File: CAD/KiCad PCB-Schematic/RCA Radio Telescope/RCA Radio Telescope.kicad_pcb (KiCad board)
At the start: 2 copper layers, 2 parts, among them U3 SKY13588-460LF, U4 SKY13588-460LF

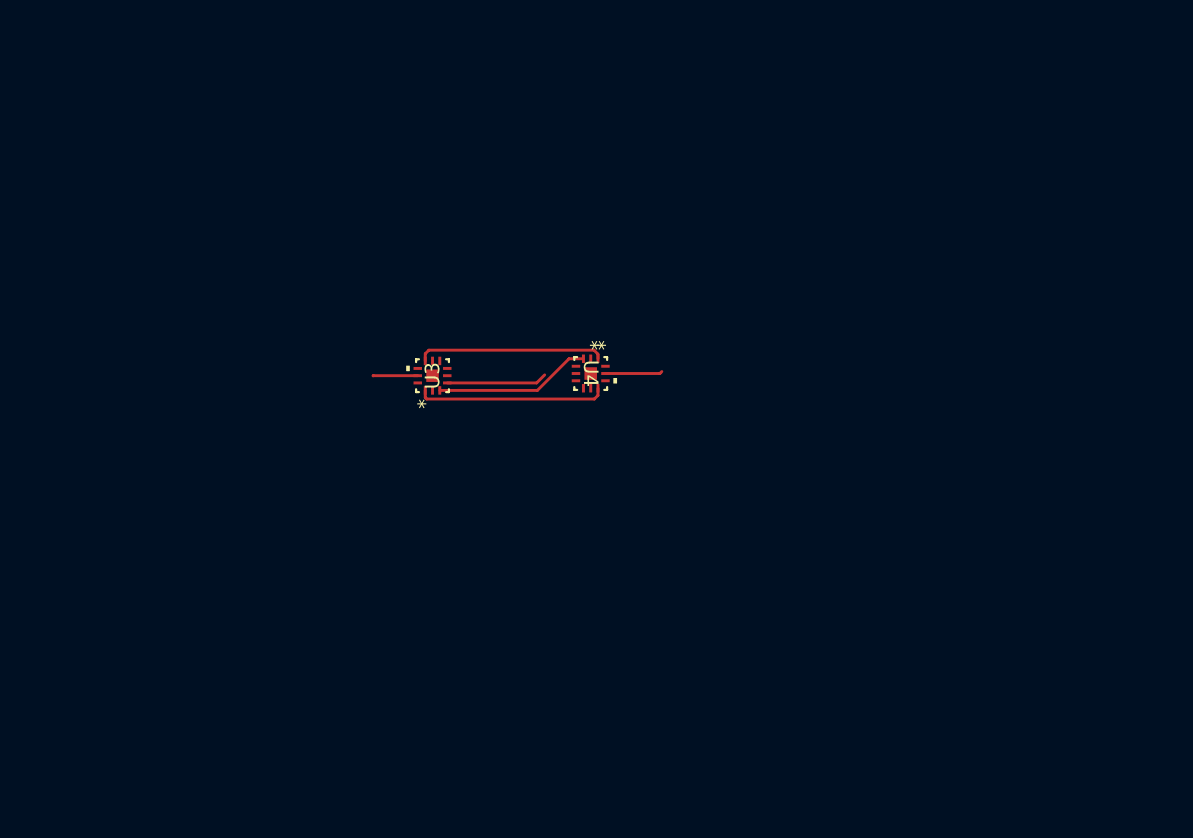
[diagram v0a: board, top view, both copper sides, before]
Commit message: Updated PowerDataDistribute schematicto v1.4
- Added components for fuses and PMOS
- Created PCB v1.0
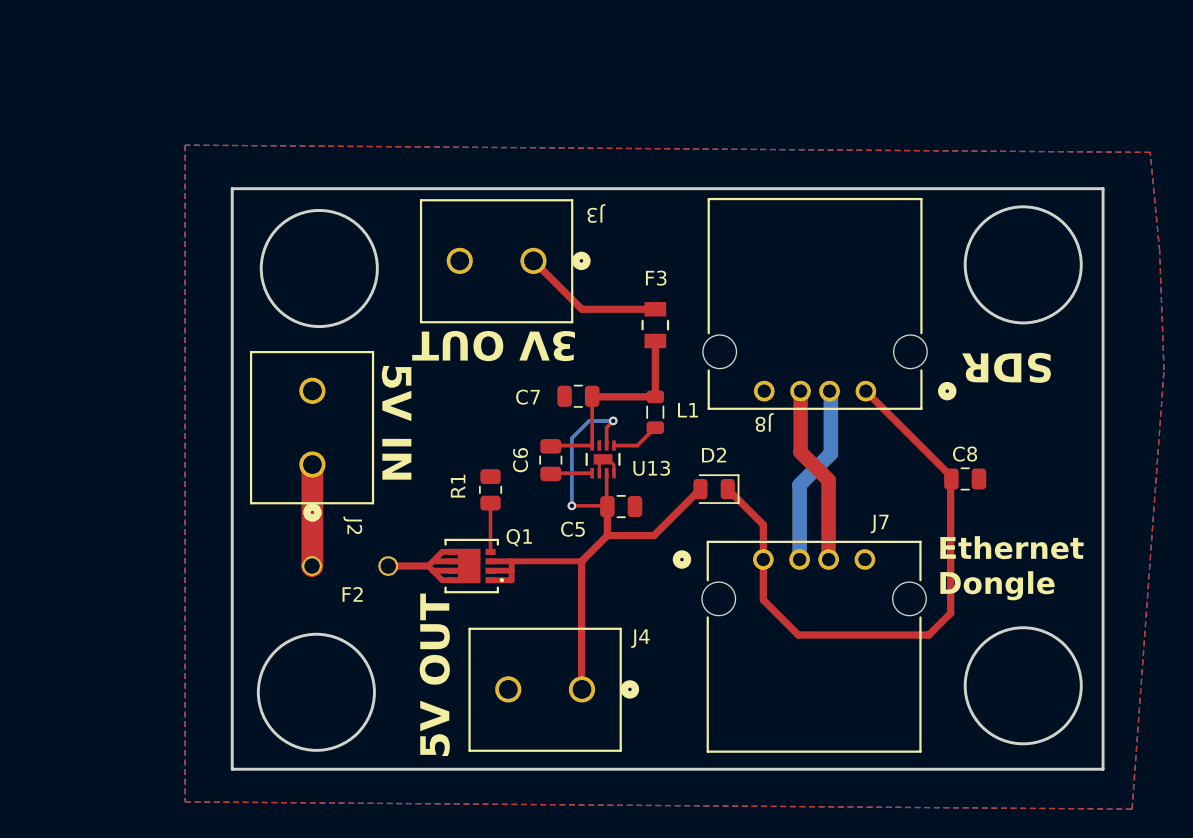
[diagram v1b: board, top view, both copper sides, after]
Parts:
- removed U3, U4: SKY13588-460LF, Library:QFN12_SKY
- added C5: 4.7 uF, Capacitor_SMD:C_0805_2012Metric, F.Cu at (52.3, 43.9)
- added C6: 560 pF, Capacitor_SMD:C_0805_2012Metric, F.Cu at (47.5, 40.7)
- added C7: 4.7 uF, Capacitor_SMD:C_0805_2012Metric, F.Cu at (49.4, 36.3)
- added C8: 10 uF, Capacitor_SMD:C_0805_2012Metric, F.Cu at (76.0, 42.0)
- added D2: D, Diode_SMD:D_0805_2012Metric, F.Cu at (58.7, 42.7)
- added F2: RGEF300K-2, Library:RGEF300K-2, F.Cu at (34.0, 52.0)
- added F3: 0ZCK0020FF2G, Library:0ZCK_BEL, F.Cu at (54.6, 31.4)
- added G***: LOGO, Library:dish, B.Cu at (46.4, 42.8)
- added J2: 5V From PoE Splitter, Library:CONN_1729128_PXC, F.Cu at (31.0, 41.0)
- added J3: 3V Out For LNA, Library:CONN_1729128_PXC, F.Cu at (46.3, 27.0)
- added J4: 5V Out For Filter Board, Library:CONN_1729128_PXC, F.Cu at (49.6, 56.5)
- added J7: USB_A, Library:CONN_AU-Y1005-2_ASM, F.Cu at (62.1, 47.6)
- added J8: USB_A, Library:CONN_AU-Y1005-2_ASM, F.Cu at (69.2, 35.9)
- added L1: 1 uH, Inductor_SMD:L_0805_2012Metric, F.Cu at (54.6, 37.4)
- added Q1: DMP2008UFG-7, Library:DMP2008UFG-7_DIO, F.Cu at (42.0, 48.0)
- added R1: 100k, Resistor_SMD:R_0805_2012Metric, F.Cu at (43.3, 42.8)
- added U13: MIC23050-SYML-TR, Library:MLF-8_ML_MCH, F.Cu at (51.0, 40.7)
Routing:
- net +5V: track 0.00 -> 45.8 mm, vias 0 -> 2
- net /PowerDataDistribute/USB_5V_IN: track 0.00 -> 40.9 mm
- net Net-(U13-SNS): track 0.00 -> 14.7 mm
- net /Filters/FILTERA_IN: track 13.0 -> 0.00 mm
- net /Filters/FILTERB_IN: track 12.9 -> 0.00 mm
- net /PowerDataDistribute/USB_D-_IN: track 0.00 -> 12.5 mm
- net /PowerDataDistribute/USB_D+_IN: track 0.00 -> 12.4 mm
- net /Filters/FILTERC_IN: track 10.8 -> 0.00 mm
- net Net-(Q1-D): track 0.00 -> 10.6 mm
- net +3V0: track 0.00 -> 9.77 mm
- net /PowerDataDistribute/VDD: track 0.00 -> 7.04 mm
- net /Filters/INT_CTRL_V1: track 6.94 -> 0.00 mm
- net /Filters/FILTER_OUT: track 3.94 -> 0.00 mm
- net Net-(Q1-G): track 0.00 -> 3.36 mm
- net Net-(U13-SW): track 0.00 -> 3.36 mm
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- added copper zone on B.Cu, net GND
- added copper zone on F.Cu, net GND
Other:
- board outline added: 60 x 40 mm
- board text added: "3V OUT"
- board text added: "5V IN"
- board text added: "5V OUT"
- board text added: "Ethernet Dongle"
- board text added: "PSU ECE Capstone Team 11 - RCA Telescope v1.0"
- board text added: "SDR"
- board text added: "Truong Le Brad Glaubitz Daniyil Kashkan Davyd Gamza Paul Nguyen"

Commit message: Updated Power/Data Distribute Board to v1.1
- Adjusted screw hole positions
- Adjusted screw terminal positions
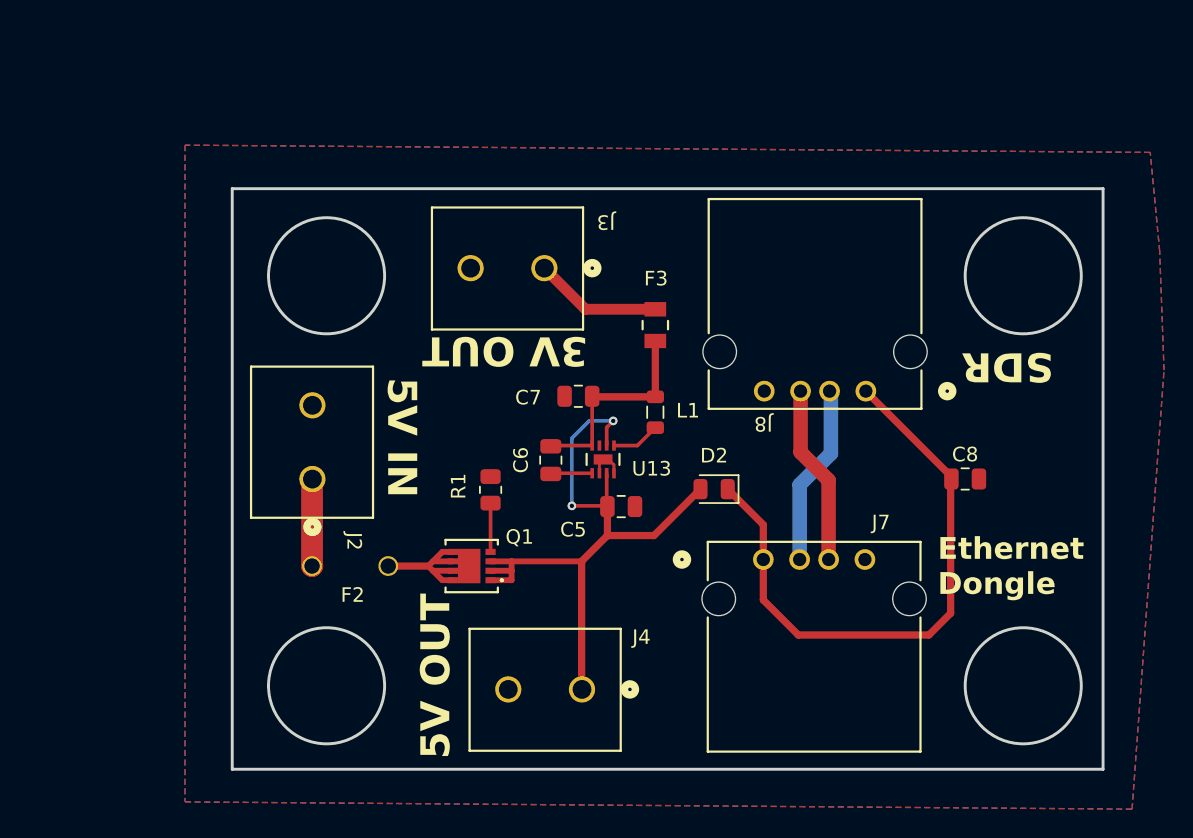
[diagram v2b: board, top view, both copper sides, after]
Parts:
- moved J2 1.00 mm to (31.0, 42.0)
- moved J3 0.90 mm to (47.0, 27.5)
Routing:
- net /PowerDataDistribute/VDD: track 7.04 -> 6.07 mm
- net +3V0: track 9.77 -> 8.82 mm
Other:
- outline, holes or cut-outs redrawn
- board text added: "PSU ECE Capstone Team 11 - RCA Telescope v1.1"
- board text removed: "PSU ECE Capstone Team 11 - RCA Telescope v1.0"
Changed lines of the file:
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@@
 		(title "Power Data Distribute PCB")
 		(date "2025-03-15")
-		(rev "1.0")
+		(rev "1.1")
 	)
 	(layers
@@
 		)
 		(property "Footprint" "Library:CONN_AU-Y1005-2_ASM"
-			(at 0 0 360)
+			(at 0 0 0)
 			(layer "F.Fab")
 			(hide yes)
@@
 		)
 		(property "Datasheet" ""
-			(at 0 0 360)
+			(at 0 0 0)
 			(layer "F.Fab")
 			(hide yes)
@@
 		)
 		(property "Description" ""
-			(at 0 0 360)
+			(at 0 0 0)
 			(layer "F.Fab")
 			(hide yes)
@@
 		(tags "capacitor")
 		(property "Reference" "C7"
-			(at 3.45 -0.0975 360)
+			(at 3.45 -0.0975 0)
 			(layer "F.SilkS")
 			(effects
@@
 		)
 		(property "Value" "4.7 uF"
-			(at 0 1.68 360)
+			(at 0 1.68 0)
 			(layer "F.Fab")
 			(effects
@@
 		)
 		(fp_text user "${REFERENCE}"
-			(at 0 0 360)
+			(at 0 0 0)
 			(layer "F.Fab")
 			(effects
@@
 		(tags "diode")
 		(property "Reference" "D2"
-			(at 0 2.3 360)
+			(at 0 2.3 0)
 			(layer "F.SilkS")
 			(effects
@@
 		)
 		(property "Value" "D"
-			(at 0 1.65 360)
+			(at 0 1.65 0)
 			(layer "F.Fab")
 			(effects
@@
 		)
 		(fp_text user "${REFERENCE}"
-			(at 0 0 360)
+			(at 0 0 0)
 			(layer "F.Fab")
 			(effects
@@
 		)
 		(property "Footprint" "Library:DMP2008UFG-7_DIO"
-			(at 0 0 360)
+			(at 0 0 0)
 			(layer "F.Fab")
 			(hide yes)
@@
 		)
 		(property "Datasheet" "https://ngspice.sourceforge.io/docs/ngspice-html-manual/manual.xhtml#cha_MOSFETs"
-			(at 0 0 360)
+			(at 0 0 0)
 			(layer "F.Fab")
 			(hide yes)
@@
 		)
 		(property "Description" "P-MOSFET transistor, drain/source/gate"
-			(at 0 0 360)
+			(at 0 0 0)
 			(layer "F.Fab")
 			(hide yes)
@@
 	(footprint "Library:CONN_1729128_PXC"
 		(layer "F.Cu")
-		(at 31.025 41.0066 90)
+		(at 31.025 42.0066 90)
 		(tags "1729128 ")
 		(property "Reference" "J2"
@@
 		)
 		(property "Footprint" "Library:CONN_1729128_PXC"
-			(at 0 0 360)
+			(at 0 0 0)
 			(layer "F.Fab")
 			(hide yes)
@@
 		)
 		(property "Datasheet" ""
-			(at 0 0 360)
+			(at 0 0 0)
 			(layer "F.Fab")
 			(hide yes)
@@
 		)
 		(property "Description" "Generic screw terminal, single row, 01x02, script generated (kicad-library-utils/schlib/autogen/connector/)"
-			(at 0 0 360)
+			(at 0 0 0)
 			(layer "F.Fab")
 			(hide yes)
@@
 	(footprint "Library:CONN_1729128_PXC"
 		(layer "F.Cu")
-		(at 46.2566 26.975001 180)
+		(at 47.0066 27.475001 180)
 		(tags "1729128 ")
 		(property "Reference" "J3"
@@
 		)
 		(property "Footprint" "Library:CONN_1729128_PXC"
-			(at 0 0 360)
+			(at 0 0 0)
 			(layer "F.Fab")
 			(hide yes)
@@
 		)
 		(property "Datasheet" ""
-			(at 0 0 360)
+			(at 0 0 0)
 			(layer "F.Fab")
 			(hide yes)
@@
 		)
 		(property "Description" "Generic screw terminal, single row, 01x02, script generated (kicad-library-utils/schlib/autogen/connector/)"
-			(at 0 0 360)
+			(at 0 0 0)
 			(layer "F.Fab")
 			(hide yes)
@@
 		(tags "capacitor")
 		(property "Reference" "C5"
-			(at -3.3 1.5975 360)
+			(at -3.3 1.5975 0)
 			(layer "F.SilkS")
 			(effects
@@
 		)
 		(property "Value" "4.7 uF"
-			(at 0.95 2.68 360)
+			(at 0.95 2.68 0)
 			(layer "F.Fab")
 			(effects
@@
 		)
 		(fp_text user "${REFERENCE}"
-			(at -3.55 2.18 360)
+			(at -3.55 2.18 0)
 			(layer "F.Fab")
 			(effects
@@
 		(tags "capacitor")
 		(property "Reference" "C8"
-			(at 0 -1.68 360)
+			(at 0 -1.68 0)
 			(layer "F.SilkS")
 			(effects
@@
 		)
 		(property "Value" "10 uF"
-			(at 0 1.68 360)
+			(at 0 1.68 0)
 			(layer "F.Fab")
 			(effects
@@
 		)
 		(fp_text user "${REFERENCE}"
-			(at 0 0 360)
+			(at 0 0 0)
 			(layer "F.Fab")
 			(effects
@@
 	)
 	(gr_circle
-		(center 31.5 27.5)
-		(end 35.5 27.5)
+		(center 32 28)
+		(end 36 28)
 		(stroke
 			(width 0.2)
@@
 	)
 	(gr_circle
-		(center 80 27.25)
-		(end 84 27.25)
+		(center 80 28)
+		(end 84 28)
 		(stroke
 			(width 0.2)
@@
 	)
 	(gr_circle
-		(center 31.3 56.7)
-		(end 27.3 56.7)
+		(center 32 56.25)
+		(end 28 56.25)
 		(stroke
 			(width 0.2)
@@
 		(layer "Edge.Cuts")
 	)
-	(gr_text "PSU ECE Capstone\nTeam 11 - RCA Telescope\nv1.0"
+	(gr_text "PSU ECE Capstone\nTeam 11 - RCA Telescope\nv1.1"
 		(at 70.3 32.8 0)
 		(layer "B.SilkS")
@@
 	)
 	(gr_text "5V IN"
-		(at 35.6 34 -90)
+		(at 36 35 -90)
 		(layer "F.SilkS")
 		(effects
@@
 	)
 	(gr_text "3V OUT"
-		(at 49.3 31.6 180)
+		(at 50 32 180)
 		(layer "F.SilkS")
 		(effects
@@
 		)
 	)
+	(dimension
+		(type aligned)
+		(layer "F.SilkS")
+		(pts
+			(xy 32 28) (xy 80 28)
+		)
+		(height 28.25)
+		(gr_text "48.0000 mm"
+			(at 56 55.15 0)
+			(layer "F.SilkS")
+			(effects
+				(font
+					(size 1 1)
+					(thickness 0.1)
+				)
+			)
+		)
+		(format
+			(prefix "")
+			(suffix "")
+			(units 3)
+			(units_format 1)
+			(precision 4)
+		)
+		(style
+			(thickness 0.1)
+			(arrow_length 1.27)
+			(text_position_mode 0)
+			(extension_height 0.58642)
+			(extension_offset 0.5) keep_text_aligned)
+	)
 	(segment
 		(start 51.800001 41.022401)
@@
 	)
 	(segment
-		(start 46.2566 26.975001)
-		(end 49.589399 30.3078)
-		(width 0.5)
+		(start 49.839399 30.3078)
+		(end 47.0066 27.475001)
+		(width 0.75)
 		(layer "F.Cu")
 		(net 3)
 	)
 	(segment
-		(start 49.589399 30.3078)
-		(end 54.65 30.3078)
-		(width 0.5)
+		(start 54.65 30.3078)
+		(end 49.839399 30.3078)
+		(width 0.75)
 		(layer "F.Cu")
 		(net 3)
@@
 	)
 	(segment
-		(start 31.025 41.0066)
-		(end 31.025 47.975)
+		(start 31 42.0316)
+		(end 31.025 42.0066)
+		(width 1.5)
+		(layer "F.Cu")
+		(net 10)
+	)
+	(segment
+		(start 31 48)
+		(end 31 42.0316)
 		(width 1.5)
 		(layer "F.Cu")

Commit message: Updated PowerData Board to v1.2
- Added zone fills for certain pins
- Added ground vias for mounting holes
- Minor readjustments to components
- Added silkscreen for voltage polarity
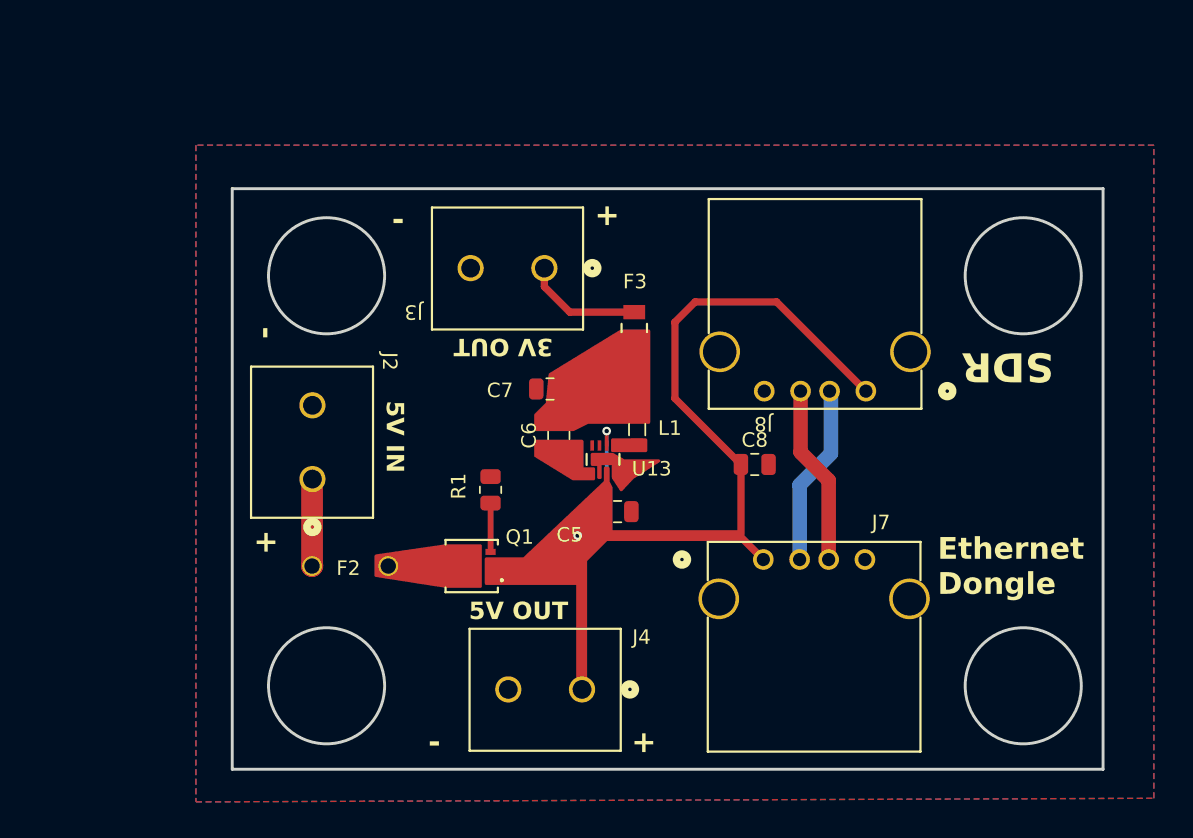
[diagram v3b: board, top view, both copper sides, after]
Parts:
- removed D2: D, Diode_SMD:D_0805_2012Metric
- moved C8 14.5 mm to (61.5, 41.0)
- moved C7 2.01 mm to (47.4, 35.8)
- moved C6 1.79 mm to (48.0, 39.0)
- moved L1 1.73 mm to (53.4, 38.6)
- moved F3 1.46 mm to (53.2, 31.6)
- moved C5 0.43 mm to (52.0, 44.2)
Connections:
- C8 pad 1: /PowerDataDistribute/USB_5V_IN -> +5V
- J7 pad 1: /PowerDataDistribute/USB_5V_IN -> +5V
- J8 pad 1: /PowerDataDistribute/USB_5V_IN -> +5V
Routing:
- net /PowerDataDistribute/USB_5V_IN: track 40.9 -> 0.00 mm
- net +5V: track 45.8 -> 66.5 mm
- net Net-(U13-SNS): track 14.7 -> 0.00 mm
- net Net-(Q1-D): track 10.6 -> 0.00 mm
- net Net-(U13-SW): track 3.36 -> 0.00 mm
- net Net-(U13-CFF): track 2.94 -> 0.00 mm
- net GND: track 2.54 -> 0.38 mm
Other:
- board text added: "+"
- board text added: "-"

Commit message: Updated Power Data Distribute PCB to v1.3
- Rearranged 5 to 3V PCB layout to fit new circuit
- Added via stitching to PCB
- Added some constraints supplied by JLCPCB
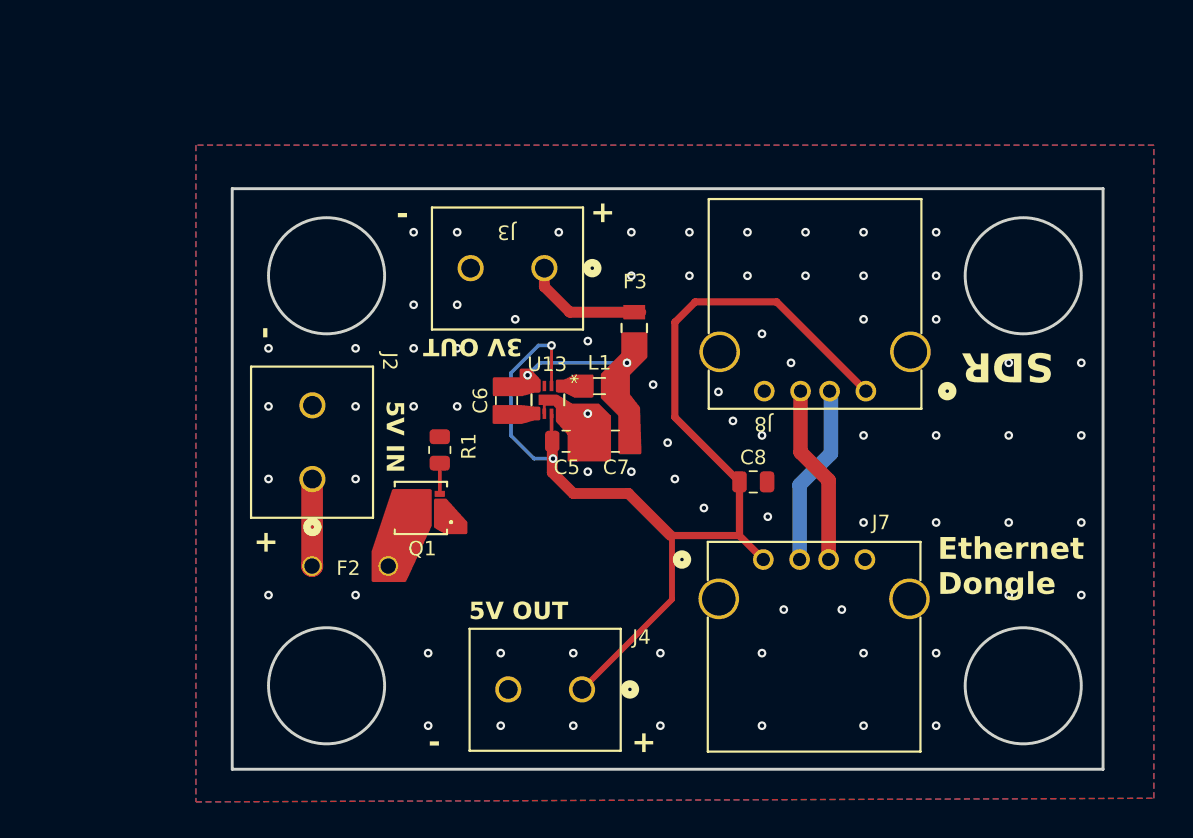
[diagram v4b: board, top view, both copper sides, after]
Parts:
- moved C5 6.01 mm to (48.5, 39.4)
- moved C7 5.76 mm to (51.9, 39.4)
- moved U13 5.59 mm to (47.2, 36.5)
- moved Q1 5.32 mm to (38.5, 44.0)
- moved R1 4.45 mm to (39.8, 40.0)
- moved C6 4.33 mm to (44.4, 36.6)
- moved L1 3.97 mm to (50.8, 35.6), turned to 0 degrees
- moved C8 1.20 mm to (61.4, 42.2)
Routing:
- net +5V: track 66.5 -> 81.2 mm
- net Net-(U13-SNS): track 0.00 -> 7.20 mm, vias 0 -> 2
- net Net-(Q1-G): track 3.36 -> 2.11 mm
- net GND: track 0.38 -> 1.44 mm, vias 0 -> 74

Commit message: V1.5 Schematic and 1.4 PCB Layout
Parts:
- added C10: 0.1uF, Capacitor_SMD:C_0805_2012Metric, F.Cu at (44.5, 48.0)
- added C11: 3.3nF, Capacitor_SMD:C_0805_2012Metric, F.Cu at (44.5, 44.2)
- added C12: 22uF, Capacitor_SMD:C_0805_2012Metric, F.Cu at (47.6, 49.4)
- added C9: 10uF, Capacitor_SMD:C_0805_2012Metric, F.Cu at (41.1, 48.0)
- added L2: 2.2uH, Inductor_SMD:L_0805_2012Metric, F.Cu at (50.5, 48.6)
- added R2: 100k, Resistor_SMD:R_0805_2012Metric, F.Cu at (51.4, 45.7)
- added U14: TPS62133RGTR, TPS62133RGTR:RGT0016C, F.Cu at (47.5, 46.4)
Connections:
- Q1 pad 3: +5V -> Net-(Q1-S)
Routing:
- net +5V: track 81.2 -> 97.5 mm
- net Net-(Q1-S): track 0.00 -> 10.9 mm
- net GND: track 1.44 -> 7.89 mm, vias 74 -> 75
- net Net-(L2-Pad1): track 0.00 -> 4.23 mm
- net Net-(U14-SS_TR): track 0.00 -> 1.97 mm
- net Net-(U14-PG): track 0.00 -> 1.58 mm
